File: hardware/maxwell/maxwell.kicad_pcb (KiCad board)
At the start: 2 copper layers, 129.5 x 59.7 mm, 82 parts, among them J1 Canbus 1, J10 SPI2_B, J11 BACKUP, J12 UART4, J13 UART5, J14 I2C1, J15 GPIO, J2 Canbus 2, J3 Neopixel, J4 BOOT0, J5 SPI2_A, J6 Programmer, J7 Dynamo Input, J8 BOOT1, J9 Battery, Q1 BSS138, Q2 PSMN5R4-25YLD, Q3 NTR1P02T1, Q4 NTR1P02T1, Q5 NTR1P02T1, U1 MCP1501, U10 MIC39102, U2 SN65HVD233, U3 ITEAD_HC-05, U5 ESP-32S, U6 FGPMMOPA6C, U7 STM32F103RETx, U8 TLP188, U9 Buck Regulator, Y1 32.768k, Y2 8M

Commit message: Updating for manufacture.
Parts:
- removed C15: 100u, coddingtonbear:CP_Tantalum_Case-D_EIA-7343-31_Milling
- removed D3: 18, adamgreig/agg-kicad/agg.pretty:DO-214AA-SMB
- removed R28, R35: 10k, coddingtonbear/coddingtonbear.pretty:0805_Milling
- removed R29, R3: 330, coddingtonbear/coddingtonbear.pretty:0805_Milling
- removed R34: 110k, coddingtonbear/coddingtonbear.pretty:0805_Milling
- removed U3: ITEAD_HC-05, pelrun/libKiCad/footprint/w_rf_modules.pretty:ITEAD_HC-05
- removed U6: FGPMMOPA6C, coddingtonbear/coddingtonbear.pretty:FGPMMOPA6C
- added J16: ESP_BM, coddingtonbear/coddingtonbear.pretty:Pin_Header_Straight_1x02_Pitch1.27mm_JMP, F.Cu at (175.8, 95.0)
- added J17: ESP_PROG, coddingtonbear/coddingtonbear.pretty:JST_XH_B03B-XH-A_03x2.50mm_Straight_LargePads, F.Cu at (191.6, 101.5)
- added J18: Supercap, coddingtonbear/coddingtonbear.pretty:JST_XH_B02B-XH-A_02x2.50mm_Straight_LargePads, F.Cu at (170.4, 84.1)
- added Q6: NTR1P02T1, coddingtonbear/coddingtonbear.pretty:SOT-23_LargePads, F.Cu at (91.1, 89.6)
- added R15: 10k, coddingtonbear/coddingtonbear.pretty:0805_Milling, F.Cu at (95.4, 90.1)
- D2: value 18 -> GS1M-LTP; footprint adamgreig/agg-kicad/agg.pretty:DO-214AA-SMB -> mcous/kicad-lib/footprints/diode.pretty:DO-214AC
- U7: footprint kicad-castellated-breakouts:QFP64-1.27MM-CASTELLATED -> kicad-castellated-breakouts:QFP64-1.27MM-CASTELLATED-VERS
- Y2: footprint nqbit/NQBit.pretty:HC-49USX_SMD -> cpavlina/kicad-pcblib/smd-non-ipc.pretty:Abracon-ABM2
- moved J5 52.6 mm to (192.5, 127.5), turned to 90 degrees
- moved J10 47.2 mm to (185.5, 127.5), turned to 90 degrees
- moved R6 34.9 mm to (189.9, 74.1)
- moved U5 33.3 mm to (185.9, 86.7)
- moved C5 15.4 mm to (194.2, 74.1), turned to 180 degrees
- moved Q2 11.8 mm to (177.0, 125.5)
- moved D2 9.01 mm to (79.3, 111.0), turned to 180 degrees
- moved R20 8.63 mm to (91.8, 100.2)
- moved Q5 8.52 mm to (87.4, 101.4)
- moved R21 8.52 mm to (95.0, 101.4)
- moved R22 8.52 mm to (90.7, 103.4)
- moved R23 8.52 mm to (92.0, 106.7)
- moved R24 8.52 mm to (94.3, 104.7)
- moved U8 6.28 mm to (77.8, 118.6), turned to 0 degrees
- moved Y2 1.70 mm to (130.7, 117.0), turned to 315 degrees
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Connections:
- BZ1 pad 1: +BATT -> VCC
- C3 pad 1: +BATT -> VCC
- C5 pad 1: +BATT -> GND
- C5 pad 2: GND -> +3V3
- D2 pad 1: DYNAMO_AC -> Net-(D2-Pad1)
- D2 pad 2: Net-(D2-Pad2) -> VCC
- J1 pad 2: +BATT -> VCC
- J10 pad 2: +BATT -> VCC
- J10 pad 3: SPI2_MOSI -> SPI2_SCK
- J10 pad 5: SPI2_SCK -> SPI2_MOSI
- J12 pad 2: +BATT -> VCC
- J13 pad 2: +BATT -> VCC
- J14 pad 2: +BATT -> VCC
- J2 pad 2: +BATT -> VCC
- J3 pad 3: +BATT -> VCC
- J5 pad 2: +BATT -> VCC
- J5 pad 3: SPI2_MOSI -> SPI2_SCK
- J5 pad 5: SPI2_SCK -> SPI2_MOSI
- Q3 pad 2: Net-(Q3-Pad2) -> Net-(D2-Pad1)
- R1 pad 1: Net-(R1-Pad1) -> CAN_DISABLE
- U10 pad 1: +BATT -> VCC
- U10 pad 2: +BATT -> VCC
- U2 pad 8: Net-(R1-Pad1) -> CAN_DISABLE
- U5 pad 23: Net-(U5-Pad23) -> BT_DO
- U5 pad 24: Net-(U5-Pad24) -> BT_DI
- U5 pad 26: Net-(U5-Pad26) -> BOOT0
- U5 pad 27: Net-(U5-Pad27) -> BT_KEY
- U5 pad 28: Net-(U5-Pad28) -> N_RST
- U7 pad 11: DYNAMO_VOLTAGE -> CAN_DISABLE
- U7 pad 15: ESP_BOOT_MODE -> BATT_SOURCE_DISABLE
- U7 pad 16: ESP_DI -> Net-(U7-Pad16)
- U7 pad 17: ESP_DO -> Net-(U7-Pad17)
- U7 pad 20: Net-(U7-Pad20) -> SPI2_CS_A
- U7 pad 21: Net-(U7-Pad21) -> SPI2_CS_B
- U7 pad 27: ~DISABLE_ESP -> Net-(U7-Pad27)
- U7 pad 34: SPI2_MOSI -> SPI2_SCK
- U7 pad 36: SPI2_SCK -> SPI2_MOSI
- U7 pad 37: SPI2_CS_B -> BT_KEY
- U7 pad 38: SPI2_CS_A -> Net-(U7-Pad38)
- U7 pad 44: BT_KEY -> ~DISABLE_ESP
- U9 pad 3: Net-(Q3-Pad2) -> Net-(D2-Pad1)
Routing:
- net +BATT: track 320.3 -> 20.2 mm, vias 5 -> 2
- net VCC: track 0.00 -> 291.6 mm, vias 0 -> 4
- net GND: track 845.2 -> 698.3 mm, vias 19 -> 12
- net BATT_SOURCE_DISABLE: track 0.00 -> 89.6 mm, vias 0 -> 2
- net CAN_DISABLE: track 0.00 -> 78.6 mm, vias 0 -> 2
- net +BACKUP: track 103.9 -> 28.0 mm, vias 2 -> 0
- net N_RST: track 3.80 -> 73.5 mm, vias 0 -> 2
- net ESP_DO: track 55.6 -> 5.86 mm
- net DYNAMO_VOLTAGE: track 49.5 -> 0.00 mm
- net Net-(D2-Pad1): track 0.00 -> 44.8 mm, vias 0 -> 2
- net ESP_DI: track 55.1 -> 10.5 mm
- net ESP_BOOT_MODE: track 45.0 -> 3.41 mm
- net DYNAMO_AC: track 74.1 -> 37.8 mm, vias 1 -> 0
- net SPI2_CS_B: track 72.6 -> 50.6 mm, vias 1 -> 0
- net GPS_DI: track 28.4 -> 7.08 mm
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- added copper zone on B.Cu, net GND
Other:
- board size 129.5 x 59.7 mm -> 124 x 60 mm
- board text added: "A"
- board text added: "B"
- board text added: "CK"
- board text added: "DI"
- board text added: "DO"
- board text added: "Maxwell v3.0 @coddingtonbear 24 June 2018"
- board text added: "RX"
- board text added: "TX"
- board text removed: "I"
- board text removed: "Maxwell v2.0 @coddingtonbear 17 February 2018"
- board text removed: "O"
- board text removed: "~~"

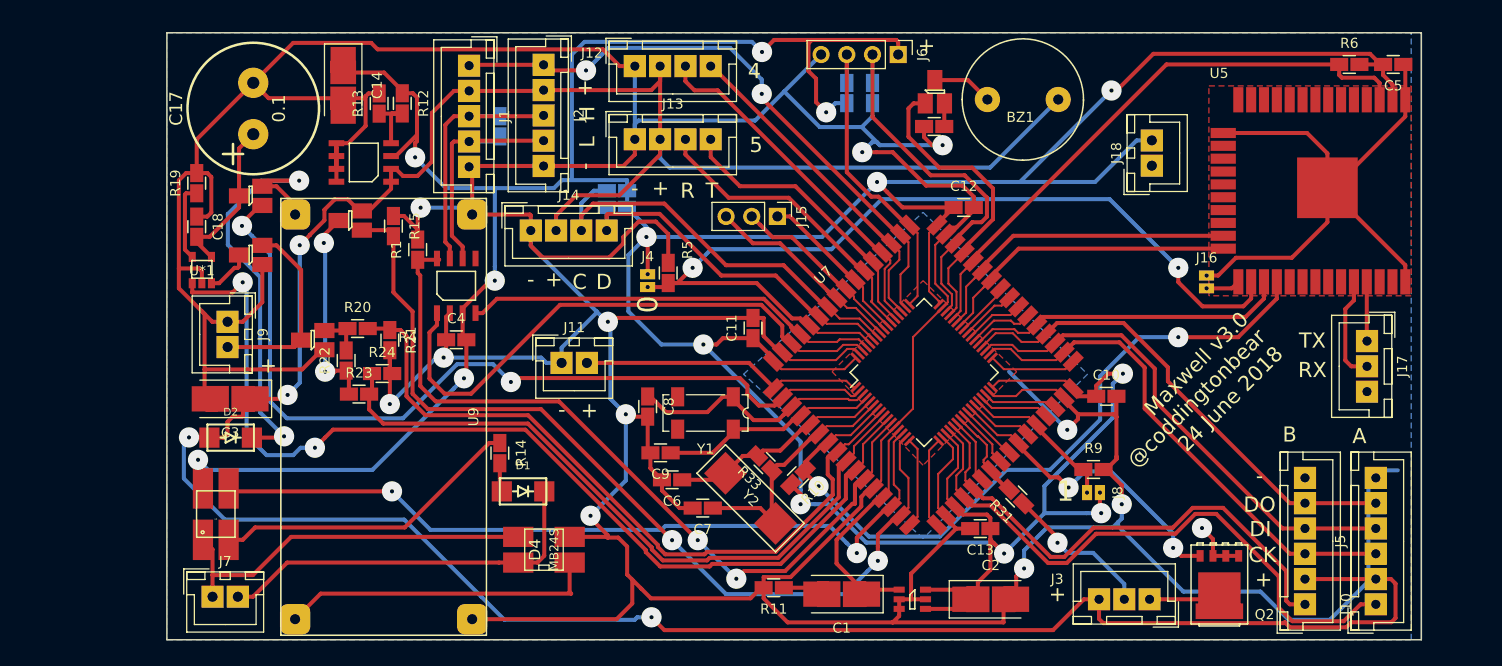
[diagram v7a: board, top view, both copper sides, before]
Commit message: Updating hardware to reference the proper libraries; adding new parts to board to support switching from dynamo input to battery.
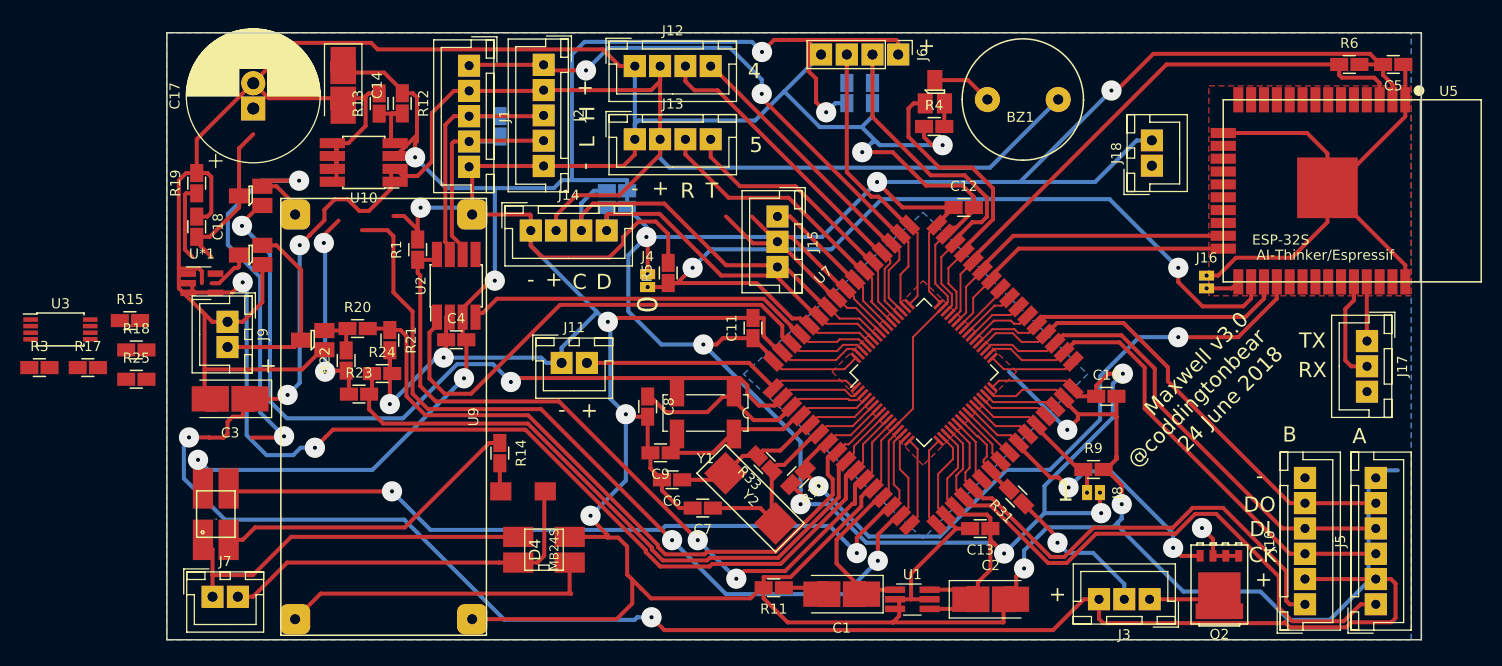
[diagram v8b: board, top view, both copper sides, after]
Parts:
- removed D2: GS1M-LTP, mcous/kicad-lib/footprints/diode.pretty:DO-214AC
- removed Q6: NTR1P02T1, coddingtonbear/coddingtonbear.pretty:SOT-23_LargePads
- added R17: 1470, coddingtonbear:0805_Milling, F.Cu at (65.2, 104.1)
- added R18: ANY, coddingtonbear:0805_Milling, F.Cu at (70.0, 102.4)
- added R25: ANY, coddingtonbear:0805_Milling, F.Cu at (70.0, 105.3)
- added R3: 500, coddingtonbear:0805_Milling, F.Cu at (60.4, 104.1)
- added U3: TPS2113, Package_SO:TSSOP-8_4.4x3mm_P0.65mm, F.Cu at (62.5, 100.3)
- BZ1: footprint coddingtonbear/coddingtonbear.pretty:12mm_buzzer -> coddingtonbear:12mm_buzzer
- C10, C11, C12, C13, C18, C4, C5, C6, C7, C8, C9, R1, R10, R11, R12, R13, R14, R16, R19, R2, R20, R21, R22, R23, R24, R31, R33, R37, R4, R5, R6, R7, R8, R9: footprint coddingtonbear/coddingtonbear.pretty:0805_Milling -> coddingtonbear:0805_Milling
- C17: footprint fruchti/fruchtilib/mod/rcl.pretty:CP_13mm_200 -> Capacitor_THT:CP_Radial_D13.0mm_P2.50mm
- C3: value 2.2u -> 22u
- D1: footprint mcous/kicad-lib/footprints/diode.pretty:DO-214AC -> coddingtonbear:DO-214AC
- D4: footprint coddingtonbear/coddingtonbear.pretty:SO-4_Milling -> coddingtonbear:SO-4_Milling
- J1, J2: footprint coddingtonbear/coddingtonbear.pretty:JST_XH_B05B-XH-A_05x2.50mm_Straight_LargePads -> coddingtonbear:JST_XH_B05B-XH-A_05x2.50mm_Straight_LargePads
- J10, J5: footprint coddingtonbear/coddingtonbear.pretty:JST_XH_B06B-XH-A_06x2.50mm_Straight_LargePads -> coddingtonbear:JST_XH_B06B-XH-A_06x2.50mm_Straight_LargePads
- J11, J18, J7, J9: footprint coddingtonbear/coddingtonbear.pretty:JST_XH_B02B-XH-A_02x2.50mm_Straight_LargePads -> coddingtonbear:JST_XH_B02B-XH-A_02x2.50mm_Straight_LargePads
- J12, J13, J14: footprint coddingtonbear/coddingtonbear.pretty:JST_XH_B04B-XH-A_04x2.50mm_Straight_LargePads -> coddingtonbear:JST_XH_B04B-XH-A_04x2.50mm_Straight_LargePads
- J15: footprint KiCad/Pin_Headers.pretty:Pin_Header_Straight_1x03_Pitch2.54mm -> coddingtonbear:JST_XH_B03B-XH-A_03x2.50mm_Straight_LargePads
- J16: footprint coddingtonbear/coddingtonbear.pretty:Pin_Header_Straight_1x02_Pitch1.27mm_JMP -> coddingtonbear:Pin_Header_Straight_1x02_Pitch1.27mm_JMP
- J17, J3: footprint coddingtonbear/coddingtonbear.pretty:JST_XH_B03B-XH-A_03x2.50mm_Straight_LargePads -> coddingtonbear:JST_XH_B03B-XH-A_03x2.50mm_Straight_LargePads
- J6: footprint KiCad/Pin_Headers.pretty:Pin_Header_Straight_1x04_Pitch2.54mm -> coddingtonbear:Pin_Header_Straight_1x04_Pitch2.54mm_LargePads
- Q1, Q3, Q4, Q5: footprint coddingtonbear/coddingtonbear.pretty:SOT-23_LargePads -> coddingtonbear:SOT-23_LargePads
- Q2: footprint coddingtonbear/coddingtonbear.pretty:PSMN5R4-25YLD -> coddingtonbear:PSMN5R4-25YLD
- R15: value 10k -> 20k; footprint coddingtonbear/coddingtonbear.pretty:0805_Milling -> coddingtonbear:0805_Milling
- U*1: footprint apexelectrix/apex-smd.pretty:SOT-23-5 -> Package_TO_SOT_SMD:SOT-23-5_HandSoldering
- U1: footprint adamgreig/agg-kicad/agg.pretty:SOT-23-6 -> Package_TO_SOT_SMD:TSOT-23-6_HandSoldering
- U10, U2: footprint adamgreig/agg-kicad/agg.pretty:SOIC-8 -> coddingtonbear:SOIC-8_3.9x4.9mm_P1.27mm_LargePads
- U5: footprint coddingtonbear/coddingtonbear.pretty:ESP-32S -> coddingtonbear:ESP-32S
- U8: footprint coddingtonbear/coddingtonbear.pretty:SO-4_Milling -> coddingtonbear:SO-4_Optocoupler_Milling
- U9: footprint coddingtonbear/coddingtonbear.pretty:BOOST_LM2596_3A -> coddingtonbear:BOOST_LM2596_3A
- Y1: footprint KiCad/Crystals.pretty:Crystal_SMD_SeikoEpson_MC306-4pin_8.0x3.2mm -> Crystal:Crystal_SMD_SeikoEpson_MC306-4Pin_8.0x3.2mm_HandSoldering
- Y2: footprint cpavlina/kicad-pcblib/smd-non-ipc.pretty:Abracon-ABM2 -> coddingtonbear:Abracon-ABM2
- moved R15 27.7 mm to (69.3, 99.5), turned to 0 degrees
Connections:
- net Net-(D2-Pad1) renamed /Power/+Dynamo_Buck
- C17 pad 1: /Power/+Dynamo -> /Power/Batt_Charge
- C18 pad 2: /Power/+Dynamo -> /Power/Batt_Charge
- D4 pad 1: Net-(D4-Pad1) -> /Power/+Dynamo
- Q3 pad 3: /Power/+Dynamo -> /Power/Batt_Charge
- R15 pad 1: GND -> /Power/+Dynamo
- R15 pad 2: BATT_SOURCE_DISABLE -> DYNAMO_VOLTAGE
- U*1 pad 4: /Power/+Dynamo -> /Power/Batt_Charge
- U7 pad 15: BATT_SOURCE_DISABLE -> DYNAMO_SOURCE_DISABLE
- U7 pad 16: Net-(U7-Pad16) -> SPI2_CS_A
- U7 pad 17: Net-(U7-Pad17) -> SPI2_CS_B
- U7 pad 20: SPI2_CS_A -> Net-(U7-Pad20)
- U7 pad 21: SPI2_CS_B -> Net-(U7-Pad21)
- U7 pad 24: Net-(U7-Pad24) -> DYNAMO_VOLTAGE
- U7 pad 25: Net-(U7-Pad25) -> DYNAMO_BUCK_VOLTAGE
- U9 pad 1: Net-(D4-Pad1) -> /Power/+Dynamo
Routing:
- net DYNAMO_SOURCE_DISABLE: track 0.00 -> 89.6 mm, vias 0 -> 2
- net BATT_SOURCE_DISABLE: track 89.6 -> 0.00 mm, vias 2 -> 0
- net Net-(D4-Pad1): track 31.5 -> 0.00 mm
- net /Power/Batt_Charge: track 0.00 -> 15.8 mm
- net /Power/+Dynamo: track 15.8 -> 31.5 mm
- net Net-(U7-Pad16): track 9.06 -> 0.00 mm
- net SPI2_CS_A: track 60.1 -> 69.2 mm
- net Net-(U7-Pad17): track 9.03 -> 0.00 mm
- net SPI2_CS_B: track 50.6 -> 59.6 mm
- net Net-(U7-Pad24): track 6.00 -> 0.00 mm
- net DYNAMO_VOLTAGE: track 0.00 -> 6.00 mm
- net Net-(U7-Pad25): track 5.81 -> 0.00 mm
- net DYNAMO_BUCK_VOLTAGE: track 0.00 -> 5.81 mm
